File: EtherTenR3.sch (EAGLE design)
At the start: 98 parts, among them IC1 MC33269DT-5.0, IC2 APX811-44UG-7, IC3 ATMEGA16U2-MU, IC4 LM358D, IC5 ATMEGA328P TQFP32, IC6 W5100SQFP80, J1 DC_2_1MM, P1 USB-FT, P2 ICSP:MAIN, P3 ICSP:USB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

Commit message: Beginning of conversion to R3
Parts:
- P1: value USB-FT -> USB-6PSMT; device freetronics-master-v1:USB-FT -> freetronics-jon:USB-6PSMT
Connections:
- new net N$3: IC3.UGND, L3.2, P1.GND, SJ1.1
- net GND: no longer IC3.UGND, L3.2, P1.GND, SJ1.1
- net N$9: now also P1.FIX1, P1.FIX2, P1.PIN1, P1.PIN2, P1.TAB1, P1.TAB2; no longer P1.SH$1, P1.SH$2, P1.SH$3, P1.SH$4

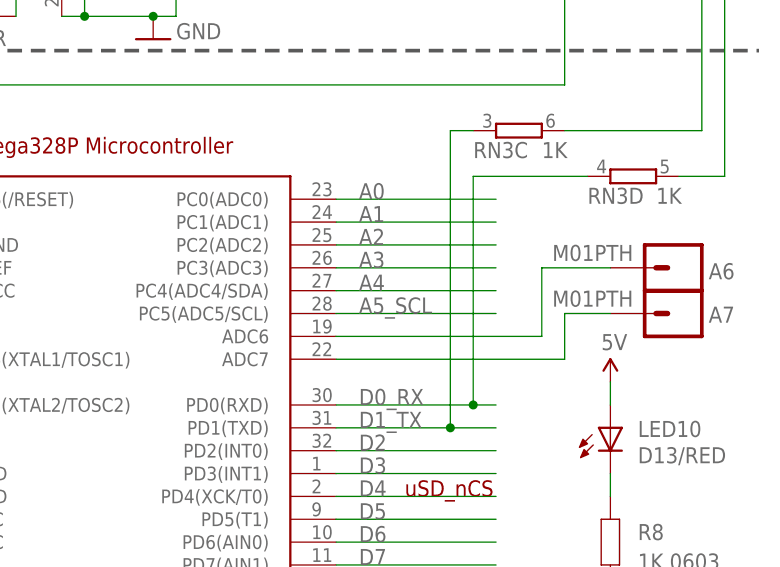
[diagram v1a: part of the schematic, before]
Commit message: Routing for R3 revision
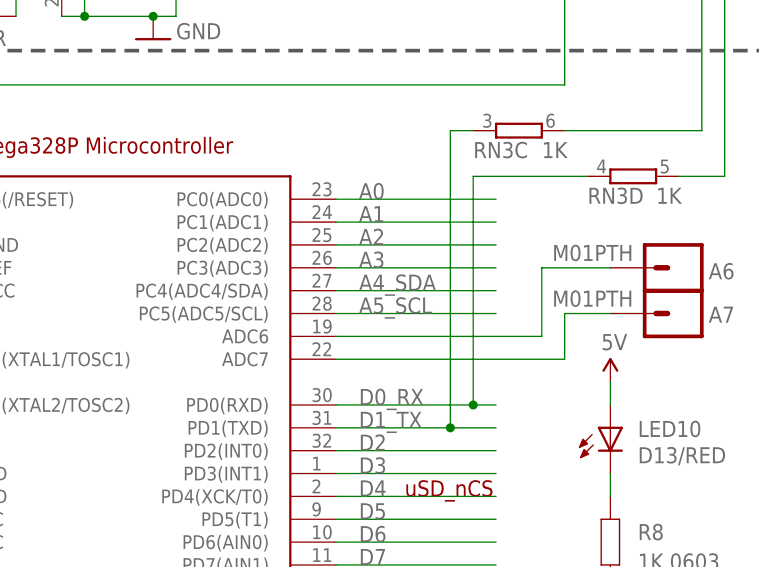
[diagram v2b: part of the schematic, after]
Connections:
- removed net A4: IC5.PC4(ADC4/SDA)
- net A4_SDA: now also IC5.PC4(ADC4/SDA)
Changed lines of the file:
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@@
-</segment>
-</net>
-<net name="A4" class="0">
-<segment>
-<wire x1="452.12" y1="73.66" x2="469.9" y2="73.66" width="0.1524" layer="91"/>
-<label x="454.66" y="73.66" size="1.778" layer="95"/>
-<pinref part="IC5" gate="G$1" pin="PC4(ADC4/SDA)"/>
 </segment>
 </net>
@@
 <label x="210.82" y="266.7" size="1.778" layer="95"/>
 </segment>
-</net>
+<segment>
+<wire x1="452.12" y1="73.66" x2="469.9" y2="73.66" width="0.1524" layer="91"/>
+<label x="454.66" y="73.66" size="1.778" layer="95"/>
+<pinref part="IC5" gate="G$1" pin="PC4(ADC4/SDA)"/>
+</segment>
+</net>

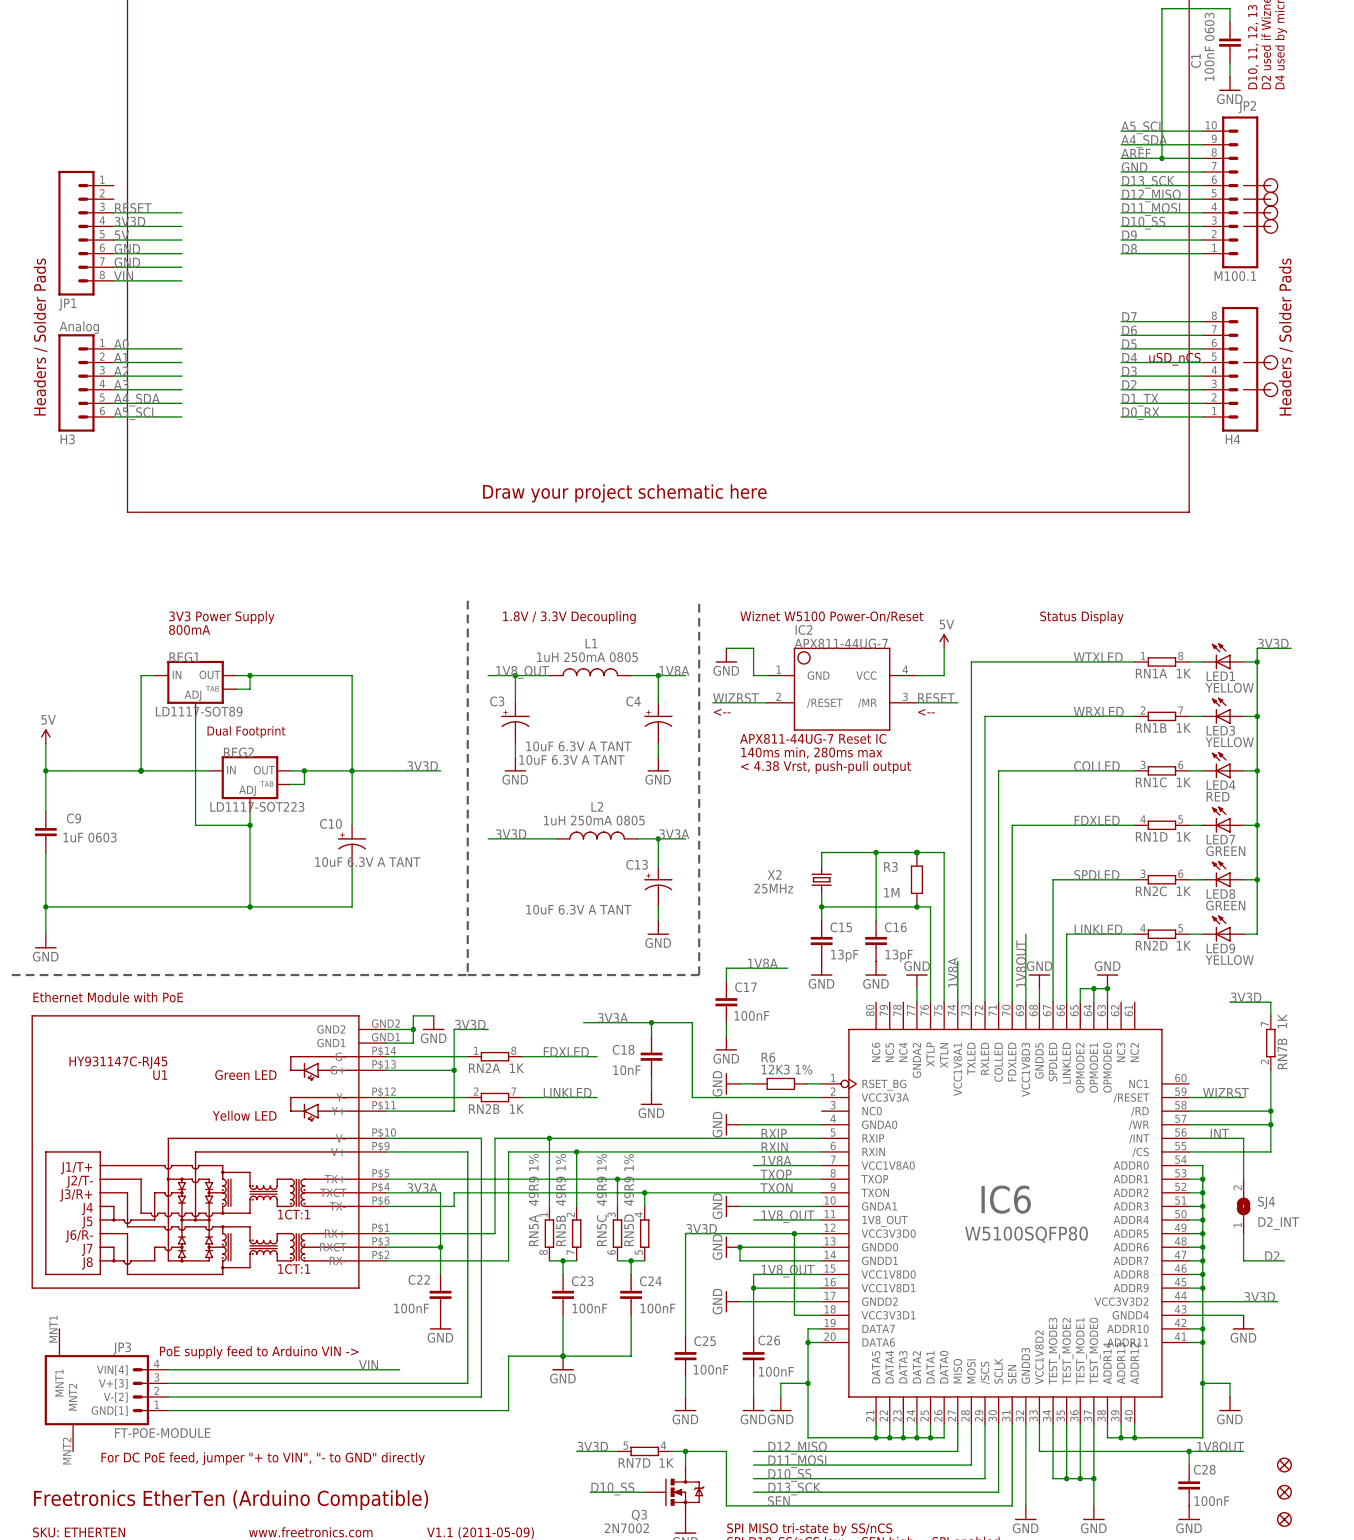
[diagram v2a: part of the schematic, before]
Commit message: More routing for R3
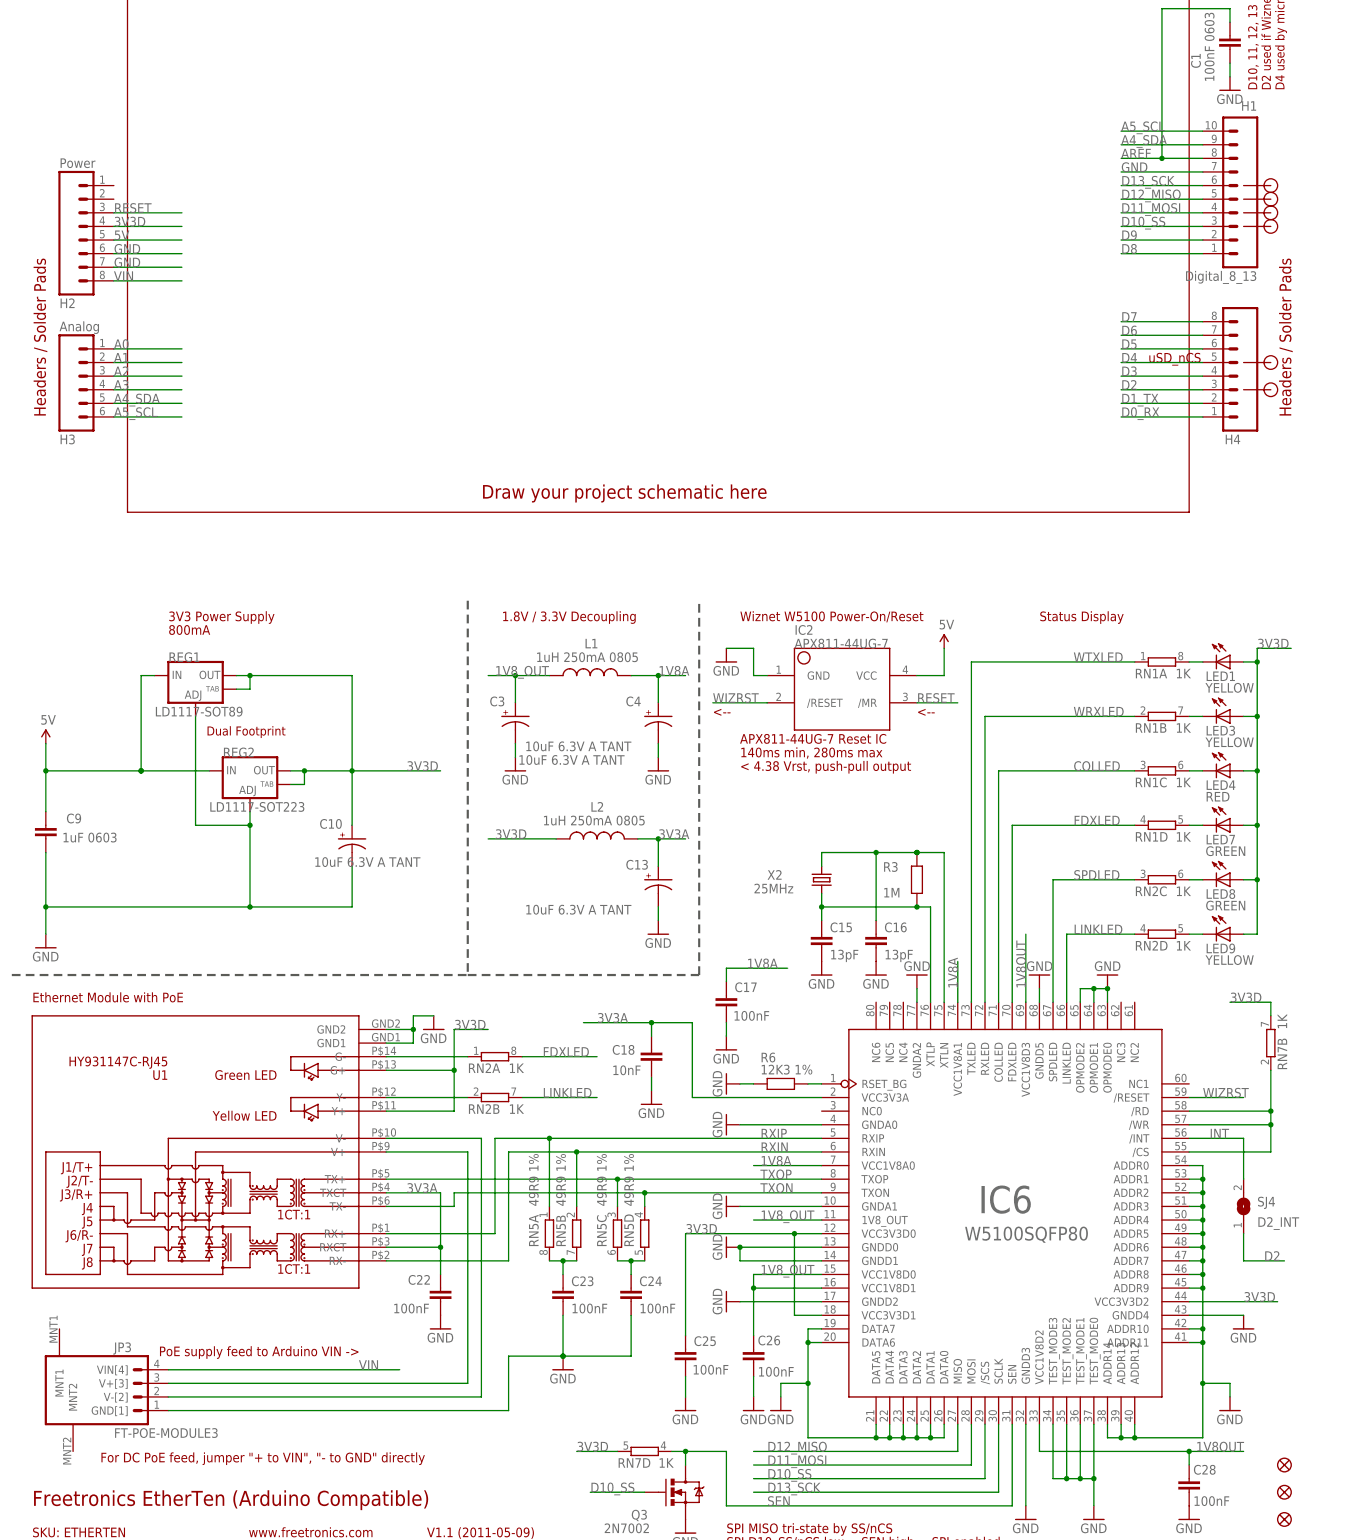
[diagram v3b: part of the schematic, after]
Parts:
- H1: value M100.1 -> Digital_8_13
- H2: value (none) -> Power
- JP3: value FT-POE-MODULE -> FT-POE-MODULE3; device freetronics-master-v1:FT-POE-MODULE -> freetronics-master-v1.1:FT-POE-MODULE3
- renumbered JP1 to H2, JP2 to H1
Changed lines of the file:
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@@
 <part name="SJ4" library="jumper" deviceset="SJ" device="" value="D2_INT"/>
 <part name="X2" library="freetronics-master-v1" deviceset="CRYSTAL" device="HC49UV" value="25MHz"/>
-<part name="JP3" library="freetronics-master-v1" deviceset="FT-POE-MODULE" device=""/>
+<part name="JP3" library="freetronics-master-v1.1" deviceset="FT-POE-MODULE" device="3"/>
 <part name="FID3" library="freetronics" deviceset="FIDUCIAL" device="1X2.5"/>
-<part name="JP1" library="freetronics-master-v1" deviceset="M08" device=""/>
-<part name="JP2" library="freetronics-original" deviceset="M10" device="0.1"/>
+<part name="H2" library="freetronics-master-v1" deviceset="M08" device="" value="Power"/>
+<part name="H1" library="freetronics-original" deviceset="M10" device="0.1" value="Digital_8_13"/>
 <part name="P1" library="freetronics-jon" deviceset="USB-6P" device="SMT"/>
 </parts>
@@
 <instance part="JP3" gate="G$1" x="22.86" y="40.64"/>
 <instance part="FID3" gate="G$1" x="241.3" y="20.32"/>
-<instance part="JP1" gate="G$1" x="17.78" y="251.46" rot="MR180"/>
-<instance part="JP2" gate="G$1" x="236.22" y="264.16" rot="MR0"/>
+<instance part="H2" gate="G$1" x="17.78" y="251.46" rot="MR180"/>
+<instance part="H1" gate="G$1" x="236.22" y="264.16" rot="MR0"/>
 <instance part="P1" gate="G$1" x="375.92" y="127" smashed="yes" rot="R180">
 <attribute name="NAME" x="375.92" y="125.73" size="2.54" layer="95" rot="R90"/>
@@
 </segment>
 <segment>
-<pinref part="JP2" gate="G$1" pin="10"/>
+<pinref part="H1" gate="G$1" pin="10"/>
 <wire x1="226.06" y1="269.24" x2="210.82" y2="269.24" width="0.2032" layer="91"/>
 <label x="210.82" y="269.24" size="1.778" layer="95"/>
@@
 <wire x1="22.86" y1="246.38" x2="35.56" y2="246.38" width="0.1524" layer="91"/>
 <label x="22.86" y="246.38" size="1.778" layer="95"/>
-<pinref part="JP1" gate="G$1" pin="6"/>
+<pinref part="H2" gate="G$1" pin="6"/>
 </segment>
 <segment>
 <wire x1="22.86" y1="243.84" x2="35.56" y2="243.84" width="0.1524" layer="91"/>
 <label x="22.86" y="243.84" size="1.778" layer="95"/>
-<pinref part="JP1" gate="G$1" pin="7"/>
+<pinref part="H2" gate="G$1" pin="7"/>
 </segment>
 <segment>
 <wire x1="210.82" y1="261.62" x2="226.06" y2="261.62" width="0.1524" layer="91"/>
 <label x="210.82" y="261.62" size="1.778" layer="95"/>
-<pinref part="JP2" gate="G$1" pin="7"/>
+<pinref part="H1" gate="G$1" pin="7"/>
 </segment>
 <segment>
@@
 <wire x1="22.86" y1="241.3" x2="35.56" y2="241.3" width="0.1524" layer="91"/>
 <label x="22.86" y="241.3" size="1.778" layer="95"/>
-<pinref part="JP1" gate="G$1" pin="8"/>
+<pinref part="H2" gate="G$1" pin="8"/>
 </segment>
 <segment>
@@
 <wire x1="22.86" y1="254" x2="35.56" y2="254" width="0.1524" layer="91"/>
 <label x="22.86" y="254" size="1.778" layer="95"/>
-<pinref part="JP1" gate="G$1" pin="3"/>
+<pinref part="H2" gate="G$1" pin="3"/>
 </segment>
 <segment>
@@
 <label x="210.82" y="264.16" size="1.778" layer="95"/>
 <pinref part="C1" gate="G$1" pin="1"/>
-<pinref part="JP2" gate="G$1" pin="8"/>
+<pinref part="H1" gate="G$1" pin="8"/>
 </segment>
 <segment>
@@
 <wire x1="210.82" y1="259.08" x2="226.06" y2="259.08" width="0.1524" layer="91"/>
 <label x="210.82" y="259.08" size="1.778" layer="95"/>
-<pinref part="JP2" gate="G$1" pin="6"/>
+<pinref part="H1" gate="G$1" pin="6"/>
 </segment>
 <segment>
@@
 <wire x1="210.82" y1="256.54" x2="226.06" y2="256.54" width="0.1524" layer="91"/>
 <label x="210.82" y="256.54" size="1.778" layer="95"/>
-<pinref part="JP2" gate="G$1" pin="5"/>
+<pinref part="H1" gate="G$1" pin="5"/>
 </segment>
 <segment>
@@
 <wire x1="226.06" y1="254" x2="210.82" y2="254" width="0.1524" layer="91"/>
 <label x="210.82" y="254" size="1.778" layer="95"/>
-<pinref part="JP2" gate="G$1" pin="4"/>
+<pinref part="H1" gate="G$1" pin="4"/>
 </segment>
 <segment>
@@
 <wire x1="210.82" y1="251.46" x2="226.06" y2="251.46" width="0.1524" layer="91"/>
 <label x="210.82" y="251.46" size="1.778" layer="95"/>
-<pinref part="JP2" gate="G$1" pin="3"/>
+<pinref part="H1" gate="G$1" pin="3"/>
 </segment>
 <segment>
@@
 <wire x1="210.82" y1="248.92" x2="226.06" y2="248.92" width="0.1524" layer="91"/>
 <label x="210.82" y="248.92" size="1.778" layer="95"/>
-<pinref part="JP2" gate="G$1" pin="2"/>
+<pinref part="H1" gate="G$1" pin="2"/>
 </segment>
 <segment>
@@
 <wire x1="210.82" y1="246.38" x2="226.06" y2="246.38" width="0.1524" layer="91"/>
 <label x="210.82" y="246.38" size="1.778" layer="95"/>
-<pinref part="JP2" gate="G$1" pin="1"/>
+<pinref part="H1" gate="G$1" pin="1"/>
 </segment>
 <segment>
@@
 <wire x1="22.86" y1="251.46" x2="35.56" y2="251.46" width="0.1524" layer="91"/>
 <label x="22.86" y="251.46" size="1.778" layer="95"/>
-<pinref part="JP1" gate="G$1" pin="4"/>
+<pinref part="H2" gate="G$1" pin="4"/>
 </segment>
 <segment>
@@
 <wire x1="22.86" y1="248.92" x2="35.56" y2="248.92" width="0.1524" layer="91"/>
 <label x="22.86" y="248.92" size="1.778" layer="95"/>
-<pinref part="JP1" gate="G$1" pin="5"/>
+<pinref part="H2" gate="G$1" pin="5"/>
 </segment>
 <segment>
@@
 </segment>
 <segment>
-<pinref part="JP2" gate="G$1" pin="9"/>
+<pinref part="H1" gate="G$1" pin="9"/>
 <wire x1="226.06" y1="266.7" x2="210.82" y2="266.7" width="0.2032" layer="91"/>
 <label x="210.82" y="266.7" size="1.778" layer="95"/>
